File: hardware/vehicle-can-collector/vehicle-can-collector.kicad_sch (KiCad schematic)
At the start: 138 parts, among them J1 OBDII Connector, J2 I2C_STANDARD, Q1 DMG2301L, Q10 MMBT3904, Q11 2N7002, Q12 2N7002, Q13 2N7002, Q14 DMG2301L, Q15 2N7002, Q16 2N7002, Q17 2N7002, Q18 2N7002, Q19 2N7002, Q2 MMBT3906, Q3 MMBT3904, Q4 DMG2301L, Q5 DMG2301L, Q6 2N7002, Q7 DMG2301L, Q8 2N7002, Q9 2N7002, U1 ATSAMC21J18A-AUT, U10 TCA9534, U11 MCP2515-xSO, U12 FT2232HL, U2 MCP2557FD-xMF, U3 LM339, U4 LMZ12001TZX-ADJ_NOPB, U5 TH8056KDC-AAA-008-RE, U6 LM317L_SOT-89, U7 LP38693MP-3.3, U8 MCP2557FD-xMF, U9 AS2333Q

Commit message: Wired up the USB connection (debug and UART output)
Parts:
- added C24, C26: 27pF, symbol Device:C
- added C25: 3.3uF, symbol Device:C
- added D20, D21: MBRA340, Diode_SMD:D_SMA, symbol Diode:MBRA340
- added J3: USB_B_Micro, Connector_USB:USB_Micro-B_Amphenol_10103594-0001LF_Horizontal, symbol Connector:USB_B_Micro
- added L1, L2: Ferrite, Inductor_SMD:L_0805_2012Metric_Pad1.05x1.20mm_HandSolder, symbol Device:L_Ferrite
- added R62: 1k, symbol Device:R
- added R63, R65, R67: 10k, symbol Device:R
- added R64: 12k 1%, symbol Device:R
- added R66: 2k2, symbol Device:R
- added U13: 93C56B, Package_SO:SOIC-8_3.9x4.9mm_P1.27mm, symbol Memory_EEPROM:93CxxB
- added Y1: 12MHz, Crystal:Crystal_HC18-U_Horizontal, symbol Device:Crystal
- C22, C23: value C -> 100nF
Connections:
- net +3V3: now also U12.20 (VCCIO), U12.31 (VCCIO), U12.42 (VCCIO), U12.50 (VREGIN), U12.56 (VCCIO), L1.2, L2.2, R62.1, R63.1, R65.1, R67.1, U13.8 (VCC)
- net +5V: now also D20.1 (K), D21.1 (K); no longer C9.1, R19.2, R26.1, U4.6 (FB)
- net GND: now also U12.1 (GND), U12.10 (AGND), U12.11 (GND), U12.13 (TEST), U12.15 (GND), U12.25 (GND), U12.35 (GND), U12.47 (GND), U12.5 (GND), U12.51 (GND), C24.2, C25.2, C26.2, J3.5 (GND), J3.6 (Shield), R64.2, U13.5 (GND); no longer C10.2
- net VBAT: now also D20.2 (A)
- net +1V8: now reaches U12.12 (VCORE)
- net +1V8: now also U12.37 (VCORE), U12.49 (VREGOUT), U12.64 (VCORE), C25.1
- net at U12.14 (~{RESET}): now also R62.2
- net at U12.2 (OSCI): now also C26.1, Y1.1
- net at U12.3 (OSCO): now also C24.1, Y1.2
- net at U12.4 (VPHY): now also L2.1
- net at U12.6 (REF): now also R64.1
- net at U12.61 (EEDATA): now also R66.2, R67.2, U13.3 (DI)
- net at U12.62 (EECLK): now also R65.2, U13.2 (SCLK)
- net at U12.63 (EECS): now also R63.2, U13.1 (CS)
- net at U12.7 (DM): now also J3.2 (D-)
- net at U12.8 (DP): now also J3.3 (D+)
- net at U12.9 (VPLL): now also L1.1
- new net: C9.1, D21.2 (A), R19.2, R26.1, U4.6 (FB)
- new net: R66.1, U13.4 (DO)
- new net VBUS: J3.1 (VBUS)
- no-connect marks 53 -> 56
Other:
- note added: "Need to add bypass on +3V3, +1V8, both isolated 3.3V"
- note added: "PROBLEM. XIN = PA14, XOUT = PA15, XIN32 = PA00, XOUT32 = PA01 Can we depend on the internal 48MHz and 32.768kHz ones?"
- note removed: "FUCK. XIN = PA14, XOUT = PA15, XIN32 = PA00, XOUT32 = PA01"
- moved on the sheet: C10, C12, C17, C22, C9, R19, R38, R45, U4

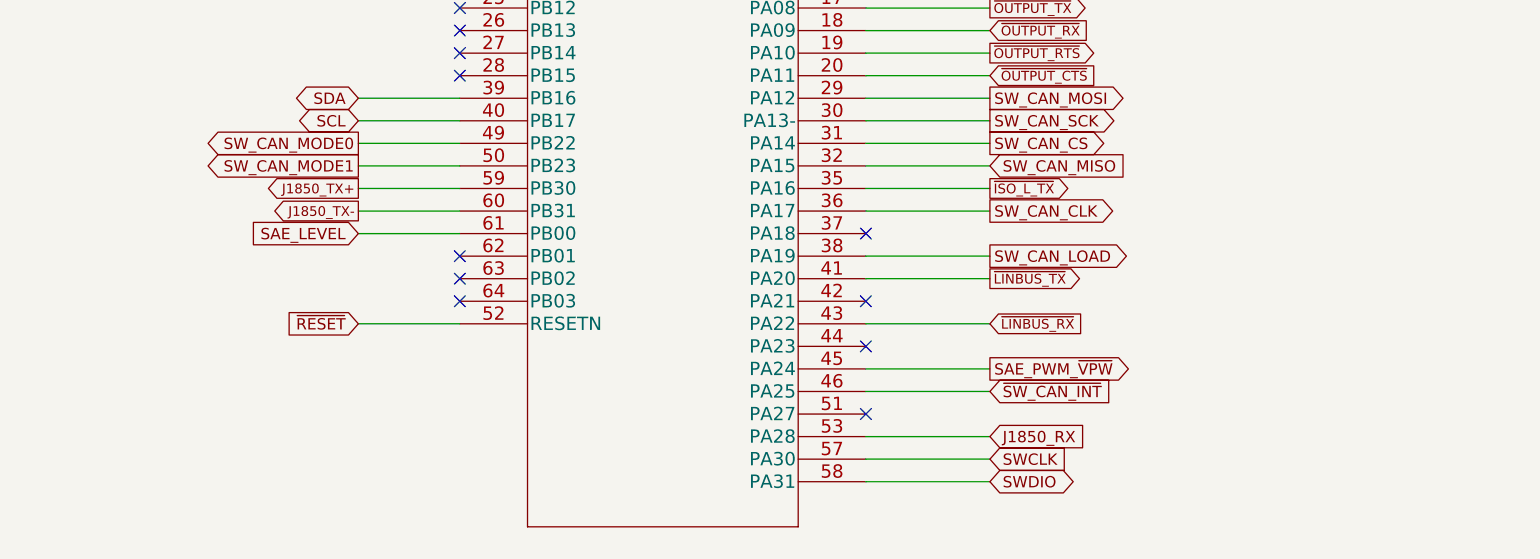
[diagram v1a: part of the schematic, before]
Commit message: Adding beginning of the structure for firmware
- copied/edit from the SAM21N Xplained Pro board
- docs not updated yet
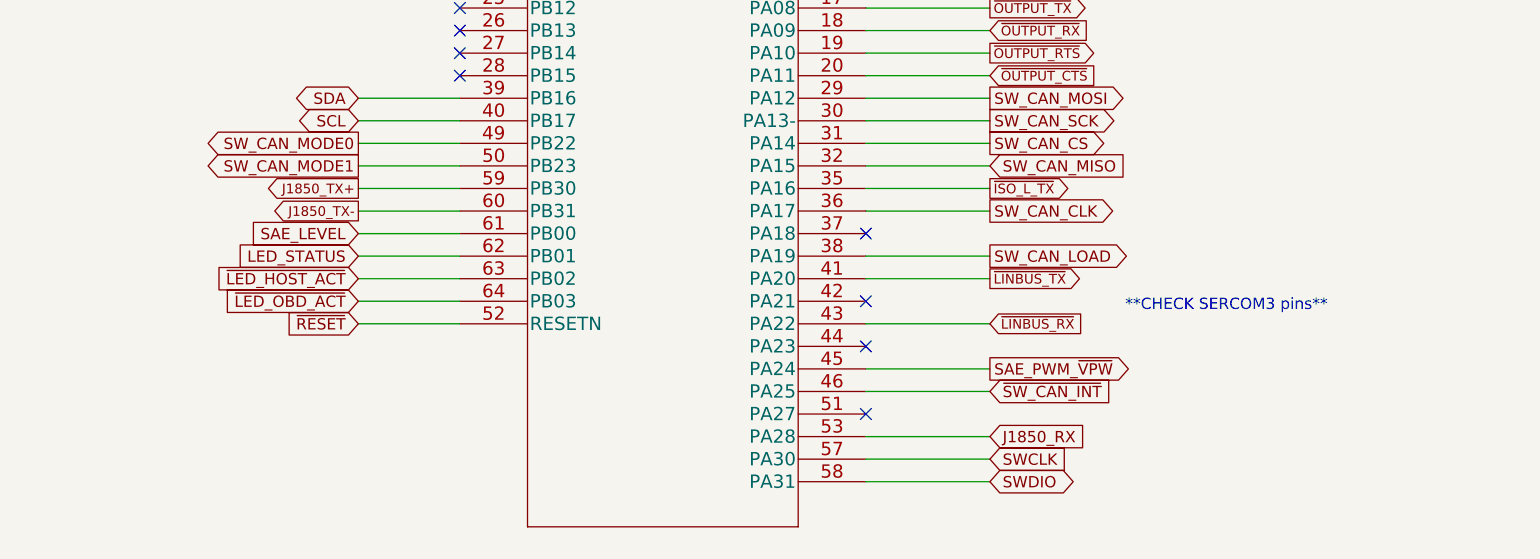
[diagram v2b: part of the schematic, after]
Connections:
- net LED_STATUS: now also U1.62 (PB01)
- net ~{LED_HOST_ACT}: now also U1.63 (PB02)
- net ~{LED_OBD_ACT}: now also U1.64 (PB03)
- no-connect marks 56 -> 53
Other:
- note added: "**CHECK SERCOM3 pins**"
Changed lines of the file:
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@@
   (no_connect (at 119.38 153.67))
   (no_connect (at 381 85.09))
-  (no_connect (at 73.66 158.75))
   (no_connect (at 381 156.21))
   (no_connect (at 73.66 115.57))
@@
   (no_connect (at 38.1 386.334))
   (no_connect (at 381 110.49))
-  (no_connect (at 73.66 156.21))
   (no_connect (at 73.66 135.89))
   (no_connect (at 381 87.63))
@@
   (no_connect (at 712.216 523.24))
   (no_connect (at 73.66 128.27))
-  (no_connect (at 73.66 161.29))
   (wire (pts (xy 62.484 517.906) (xy 62.484 520.7))
     (stroke (width 0) (type default) (color 0 0 0 0))
@@
     (stroke (width 0) (type default) (color 0 0 0 0))
   )
+  (wire (pts (xy 62.23 156.21) (xy 73.66 156.21))
+    (stroke (width 0) (type default) (color 0 0 0 0))
+  )
   (wire (pts (xy 538.48 455.93) (xy 574.04 455.93))
     (stroke (width 0) (type default) (color 0 0 0 0))
@@
     (stroke (width 0) (type default) (color 0 0 0 0))
   )
+  (wire (pts (xy 62.23 158.75) (xy 73.66 158.75))
+    (stroke (width 0) (type default) (color 0 0 0 0))
+  )
   (wire (pts (xy 432.562 501.65) (xy 437.642 501.65))
+    (stroke (width 0) (type default) (color 0 0 0 0))
+  )
+  (wire (pts (xy 62.23 161.29) (xy 73.66 161.29))
     (stroke (width 0) (type default) (color 0 0 0 0))
   )
@@
   )
   (text "+3V3 @ 500mA" (at 196.596 509.524 0)
+    (effects (font (size 1.27 1.27)) (justify left bottom))
+  )
+  (text "**CHECK SERCOM3 pins**" (at 148.59 162.56 0)
     (effects (font (size 1.27 1.27)) (justify left bottom))
   )
@@
   (global_label "LED_STATUS" (shape input) (at 26.67 518.16 180) (fields_autoplaced)
     (effects (font (size 1.27 1.27)) (justify right))
-    (property "Intersheet References" "${INTERSHEET_REFS}" (id 0) (at 0 0 0)
-      (effects (font (size 1.27 1.27)) hide)
+    (property "Intersheet References" "${INTERSHEET_REFS}" (id 0) (at 13.1577 518.0806 0)
+      (effects (font (size 1.27 1.27)) (justify right) hide)
     )
   )
@@
     )
   )
+  (global_label "LED_STATUS" (shape input) (at 62.23 156.21 180) (fields_autoplaced)
+    (effects (font (size 1.27 1.27)) (justify right))
+    (property "Intersheet References" "${INTERSHEET_REFS}" (id 0) (at 48.7177 156.1306 0)
+      (effects (font (size 1.27 1.27)) (justify right) hide)
+    )
+  )
   (global_label "SW_CAN_MISO" (shape output) (at 433.07 448.31 180) (fields_autoplaced)
     (effects (font (size 1.27 1.27)) (justify right))
@@
     )
   )
+  (global_label "~{LED_HOST_ACT}" (shape input) (at 62.23 158.75 180) (fields_autoplaced)
+    (effects (font (size 1.27 1.27)) (justify right))
+    (property "Intersheet References" "${INTERSHEET_REFS}" (id 0) (at 46.3591 158.6706 0)
+      (effects (font (size 1.27 1.27)) (justify right) hide)
+    )
+  )
   (global_label "~{SW_CAN_RESET}" (shape output) (at 494.03 408.94 0) (fields_autoplaced)
     (effects (font (size 1.27 1.27)) (justify left))
@@
     )
   )
+  (global_label "~{LED_OBD_ACT}" (shape input) (at 62.23 161.29 180) (fields_autoplaced)
+    (effects (font (size 1.27 1.27)) (justify right))
+    (property "Intersheet References" "${INTERSHEET_REFS}" (id 0) (at 47.3268 161.2106 0)
+      (effects (font (size 1.27 1.27)) (justify right) hide)
+    )
+  )

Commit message: Renamed datasheets, split schematic into sheets, added uSD card
- also rearranged IOs to fit in the oscillators and another SPI port for
  the microSD card
- will redo the devicetree shortly
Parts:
- removed C1, C13, C20, C21, C3: 100nF 25V, symbol Device:C
- removed C10: 100uF 6V3, symbol Device:C
- removed C11, C15, C16, C5: 1uF 6V3, symbol Device:C
- removed C12: 10uF 25V, symbol Device:C
- removed C14: 150pF, symbol Device:C
- removed C17: 10nF 16V, symbol Device:C
- removed C18, C19, C7, C8: 560pF, symbol Device:C
- removed C2: 47uF 25V Ta, symbol Device:CP
- removed C22, C23: 100nF, symbol Device:C
- removed C24, C26: 27pF, symbol Device:C
- removed C25: 3.3uF, symbol Device:C
- removed C4: 10nF 100V, symbol Device:C
- removed C6: 1uF 25V, symbol Device:C
- removed C9: 1nF 6V3, symbol Device:C
- removed D1: BZX884B9V1L, Diode_SMD:D_0402_1005Metric_Pad0.77x0.64mm_HandSolder, symbol Device:D_Zener
- removed D10, D14: PESD1CAN, SOT23-3, symbol SparkFun-DiscreteSemi:PESD1CAN
- removed D11, D15, D9: BAT46, Diode_THT:D_DO-35_SOD27_P7.62mm_Horizontal, symbol Diode:BAT46
- removed D12, D13: BAT54W, Package_TO_SOT_SMD:SOT-323_SC-70, symbol Diode:BAT54W
- removed D16, D17, D18: LED, symbol Device:LED
- removed D19: BAT54AW, Package_TO_SOT_SMD:SOT-323_SC-70, symbol Diode:BAT54AW
- removed D2: BZX884B20L, Diode_SMD:D_0402_1005Metric_Pad0.77x0.64mm_HandSolder, symbol Device:D_Zener
- removed D20, D21, D5: MBRA340, Diode_SMD:D_SMA, symbol Diode:MBRA340
- removed D3, D4: MMBZ27VALT116, DIO_MMBZ1_ROM, symbol UltraLibrarian:MMBZ27VALT116
- removed D6, D7: BZT52B16, Diode_SMD:D_SOD-123, symbol Diode:BZT52Bxx
- removed D8: MMBZ27VCLT1, SOT23-3, symbol SparkFun-DiscreteSemi:MMBZ27VCLT1
- removed F1: 2A Polyfuse, symbol Device:Polyfuse
- removed J1: OBDII Connector, OBDII, symbol SparkFun-Connectors:OBDII
- removed J2: I2C_STANDARD, Connector_JST:JST_PH_S4B-PH-K_1x04_P2.00mm_Horizontal, symbol SparkFun-Connectors:I2C_STANDARD
- removed J3: USB_B_Micro, Connector_USB:USB_Micro-B_Amphenol_10103594-0001LF_Horizontal, symbol Connector:USB_B_Micro
- removed L1, L2: Ferrite, Inductor_SMD:L_0805_2012Metric_Pad1.05x1.20mm_HandSolder, symbol Device:L_Ferrite
- removed Q1, Q14, Q4, Q5, Q7: DMG2301L, Package_TO_SOT_SMD:SOT-23, symbol Transistor_FET:DMG2301L
- removed Q10, Q3: MMBT3904, Package_TO_SOT_SMD:SOT-23, symbol Transistor_BJT:MMBT3904
- removed Q11, Q12, Q13, Q15, Q16, Q17, Q18, Q19, Q6, Q8, Q9: 2N7002, Package_TO_SOT_SMD:SOT-23, symbol Transistor_FET:2N7002
- removed Q2: MMBT3906, Package_TO_SOT_SMD:SOT-23, symbol Transistor_BJT:MMBT3906
- removed R1: 62k 1%, symbol Device:R
- removed R10, R11, R47, R48: 100, symbol Device:R
- removed R12, R49: 4k7, symbol Device:R
- removed R13, R14, R15, R16, R18, R24, R25, R28, R29, R30, R39, R4, R40, R44, R46, R51, R59, R60, R63, R65, R67: 10k, symbol Device:R
- removed R17, R66: 2k2, symbol Device:R
- removed R19: 4k3, symbol Device:R
- removed R2, R58: 10k 1%, symbol Device:R
- removed R20, R23, R3, R31, R42, R43, R55, R56, R7, R8: 100k, symbol Device:R
- removed R21: 1k5, symbol Device:R
- removed R22, R6: 510 500mW, symbol Device:R
- removed R26: 820, symbol Device:R
- removed R27, R32, R34, R5, R62, R9: 1k, symbol Device:R
- removed R33: 6k49 1%, symbol Device:R
- removed R35: 82k, symbol Device:R
- removed R36: 130 1W, symbol Device:R
- removed R37: 237 1%, symbol Device:R
- removed R38: 33k, symbol Device:R
- removed R41: 866 1%, symbol Device:R
- removed R45: 5k1, symbol Device:R
- removed R50: 374 1%, symbol Device:R
- removed R52, R53, R54: 330, symbol Device:R
- removed R57: 18k2 1%, symbol Device:R
- removed R61: 270, symbol Device:R
- removed R64: 12k 1%, symbol Device:R
- removed RN1: 10k, Resistor_THT:R_Array_SIP9, symbol Device:R_Network08
- removed U1: ATSAMC21J18A-AUT, TQFP64_10x10MC_MCH, symbol UltraLibrarian:ATSAMC21J18A-AUT
- removed U10: TCA9534, Package_SO:TSSOP-16_4.4x5mm_P0.65mm, symbol Interface_Expansion:TCA9534
- removed U11: MCP2515-xSO, Package_SO:SOIC-18W_7.5x11.6mm_P1.27mm, symbol Interface_CAN_LIN:MCP2515-xSO
- removed U12: FT2232HL, Package_QFP:LQFP-64_10x10mm_P0.5mm, symbol Interface_USB:FT2232HL
- removed U13: 93C56B, Package_SO:SOIC-8_3.9x4.9mm_P1.27mm, symbol Memory_EEPROM:93CxxB
- removed U2, U8: MCP2557FD-xMF, Package_DFN_QFN:DFN-8-1EP_3x3mm_P0.65mm_EP1.55x2.4mm, symbol Interface_CAN_LIN:MCP2557FD-xMF
- removed U3: LM339, TQFP64_10x10MC_MCH, symbol Comparator:LM339
- removed U4: LMZ12001TZX-ADJ_NOPB, TZA07A, symbol UltraLibrarian:LMZ12001TZX-ADJ_NOPB
- removed U5: TH8056KDC-AAA-008-RE, MEL_SOIC-8_MEL, symbol UltraLibrarian:TH8056KDC-AAA-008-RE
- removed U6: LM317L_SOT-89, Package_TO_SOT_SMD:SOT-89-3, symbol Regulator_Linear:LM317L_SOT-89
- removed U7: LP38693MP-3.3, Package_TO_SOT_SMD:SOT-223-5, symbol Regulator_Linear:LP38693MP-3.3
- removed U9: AS2333Q, Package_SO:SOIC-8_3.9x4.9mm_P1.27mm, symbol Device:Opamp_Dual
- removed Y1: 12MHz, Crystal:Crystal_HC18-U_Horizontal, symbol Device:Crystal
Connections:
- no-connect marks 53 -> 0
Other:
- added sheet Analog Inputs (analog.kicad_sch)
- added sheet CAN Bus (canbus.kicad_sch)
- added sheet ISO (iso.kicad_sch)
- added sheet J1850 (j1850.kicad_sch)
- added sheet OBDII (obd2.kicad_sch)
- added sheet Peripherals (peripherals.kicad_sch)
- added sheet Power (power.kicad_sch)
- added sheet processor (processor.kicad_sch)
- note removed: "**CHECK SERCOM3 pins**"
- note removed: "+3V3 @ 500mA"
- note removed: "1.25V reference 5.02V for PWM 6.99V for VPW"
- note removed: "1.667V @ 12V 2.5V @ 18V 2.777V max @ 20V (zener)"
- note removed: "1.773V @ 5V 2.482V @ 7V 3.262V max @ 9.1V (zener)"
- note removed: "5V @ 1A"
- note removed: "High-Speed CAN Transceiver"
- note removed: "I2C Address 0x20"
- note removed: "ISO/K-Line Receiver"
- note removed: "ISO/K-Line Transmitter"
- note removed: "ISO/L-Line Transmitter"
- note removed: "J1850 PWM Receiver"
- note removed: "J1850 Rx Multiplexor"
- note removed: "J1850 Transmitter"
- note removed: "J1850 VPW Receiver"
- note removed: "Medium-Speed CAN Transceiver"
- note removed: "Need to add bypass on +3V3, +1V8, both isolated 3.3V"
- note removed: "PROBLEM. XIN = PA14, XOUT = PA15, XIN32 = PA00, XOUT32 = PA01 Can we depend on the internal 48MHz and 32.768kHz ones?"
- note removed: "QWIIC (I2C) connector Connect to SparkFun GPS module (I2C Addr 0x10)"
- note removed: "SERCOM0 USART - K-Line on PA04-07 SERCOM1 USART - L-Line on PA16-19 SERCOM2 USART - OUTPUT on PA08-11 SERCOM3 USART - LINBus on PA20-23 SERCOM4 SPI - SW-CAN on PA12-15 SERCOM5 I2C - SW-CAN on PB16-17 GCLKIO3 - SW-CAN clock gen on PA17 TCC0 - SAE J1850 I/O on PB30-31 EXTINT8 - SAE J1850 Rx on PA28 EXTINT13 - SW-CAN IRQ on PA25 AIN0 - SAE_LEVEL on PB00 (ADC1) AIN7 - BAT_LEVEL on PA07 (ADC0) SWCLK/S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"
- note removed: "Single-Wire CAN Controller"
- note removed: "Single-Wire CAN Transceiver"

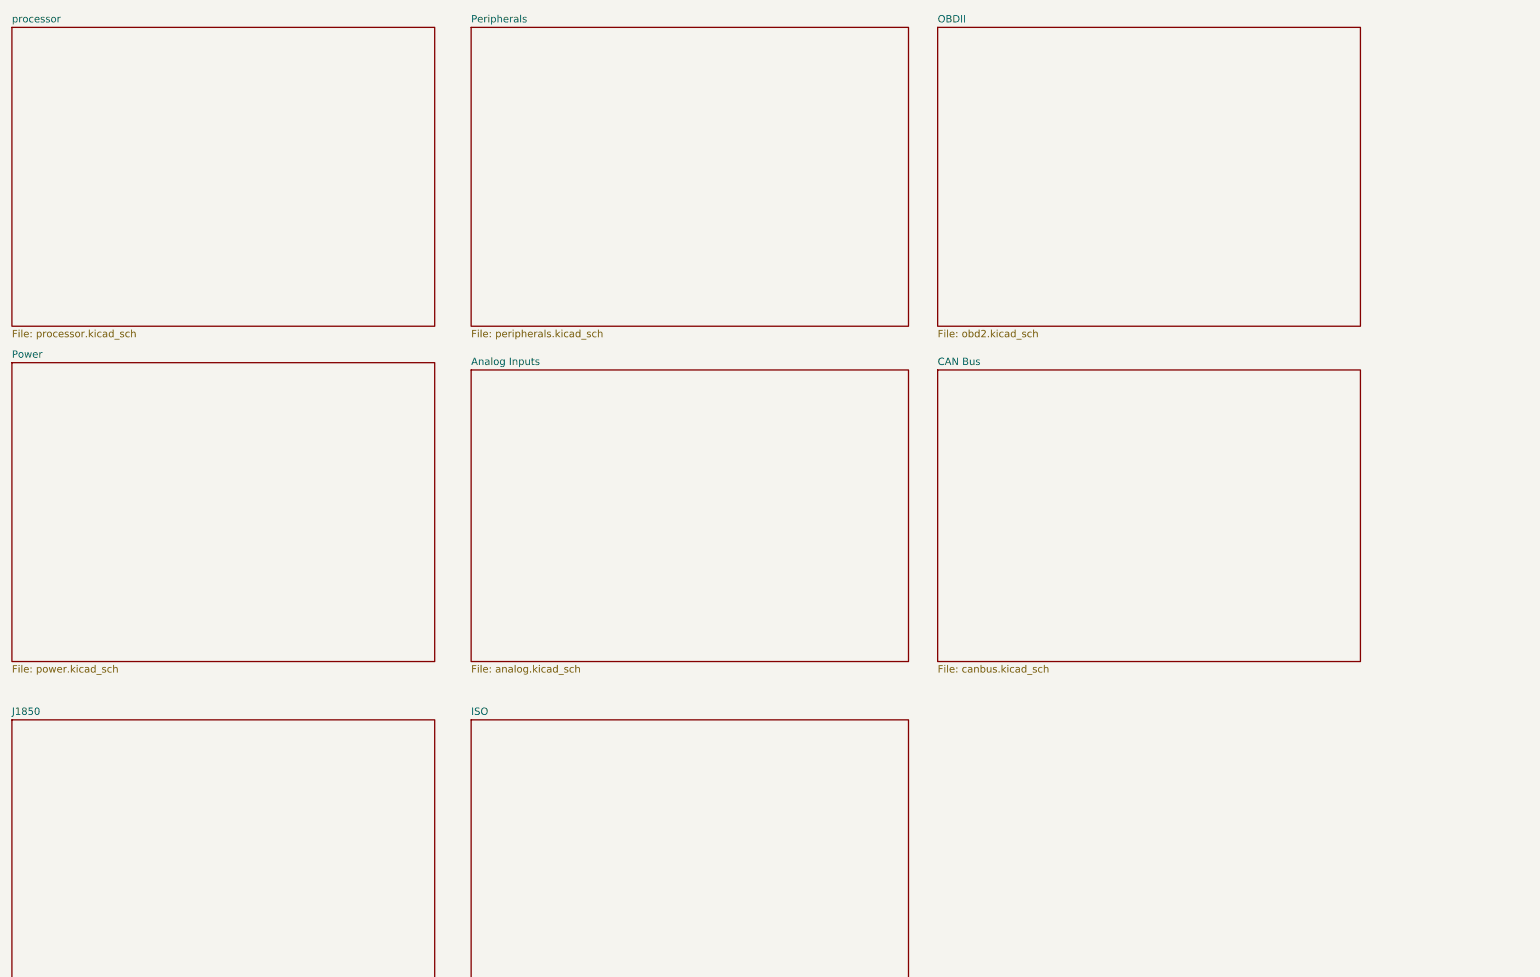
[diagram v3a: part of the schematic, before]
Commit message: Added decoupling, more LEDs, update dts
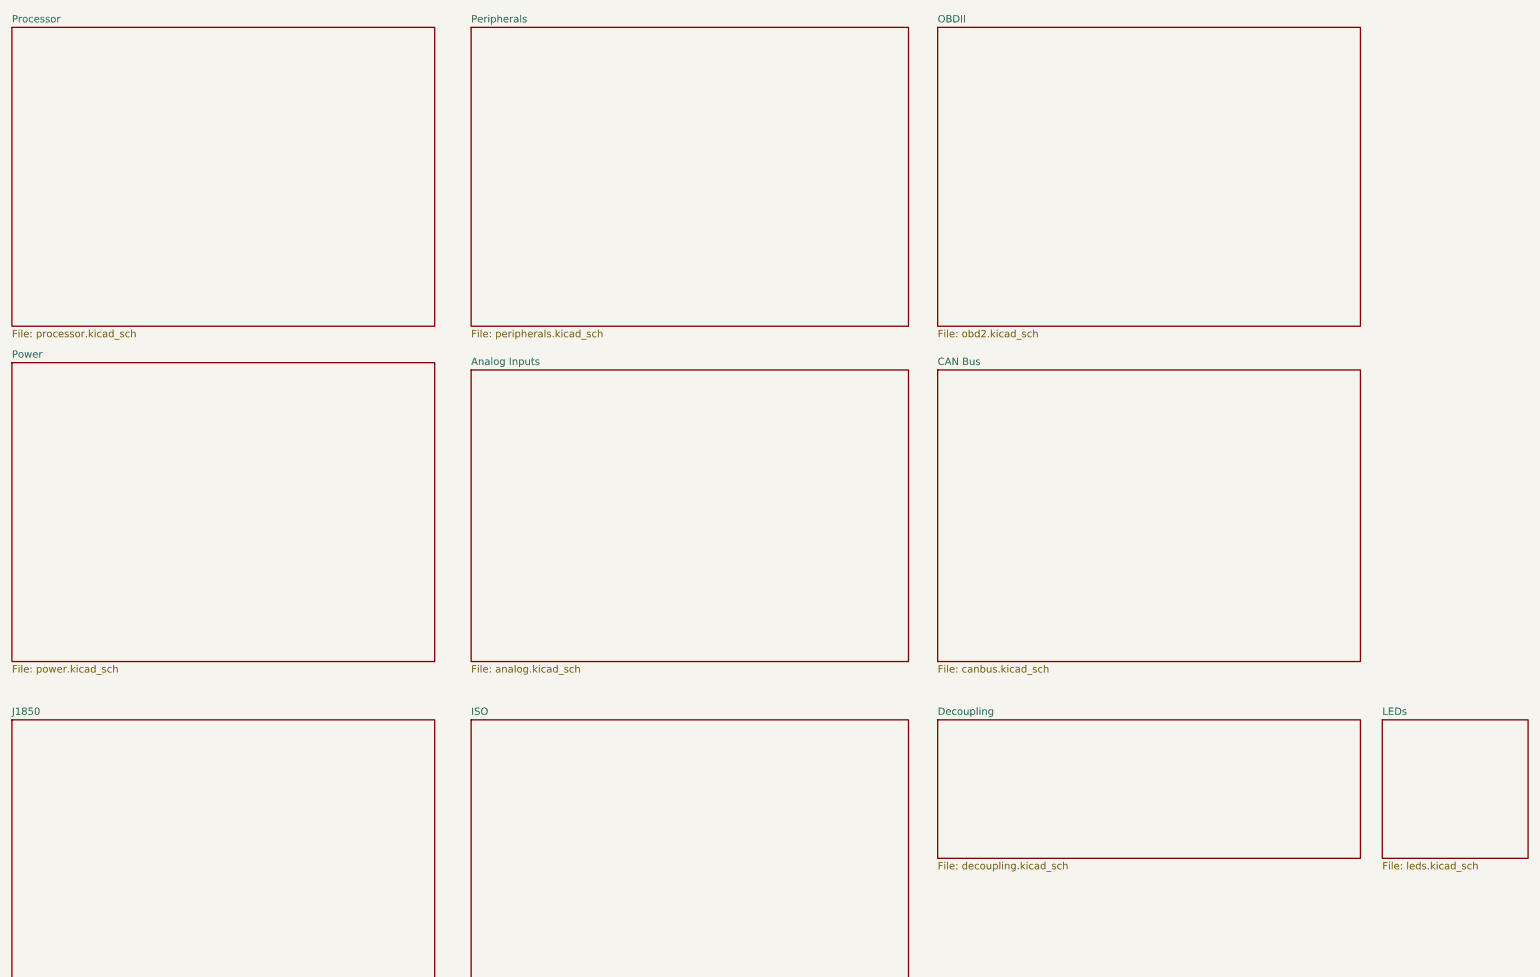
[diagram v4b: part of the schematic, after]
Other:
- sheet processor renamed Processor
- added sheet Decoupling (decoupling.kicad_sch)
- added sheet LEDs (leds.kicad_sch)
- company: (none) -> Gavin Hurlbut
- title: (none) -> Vehicle CAN Collector
